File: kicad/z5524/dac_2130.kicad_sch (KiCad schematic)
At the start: 31 parts, among them U3 TL072, U4 AD5328

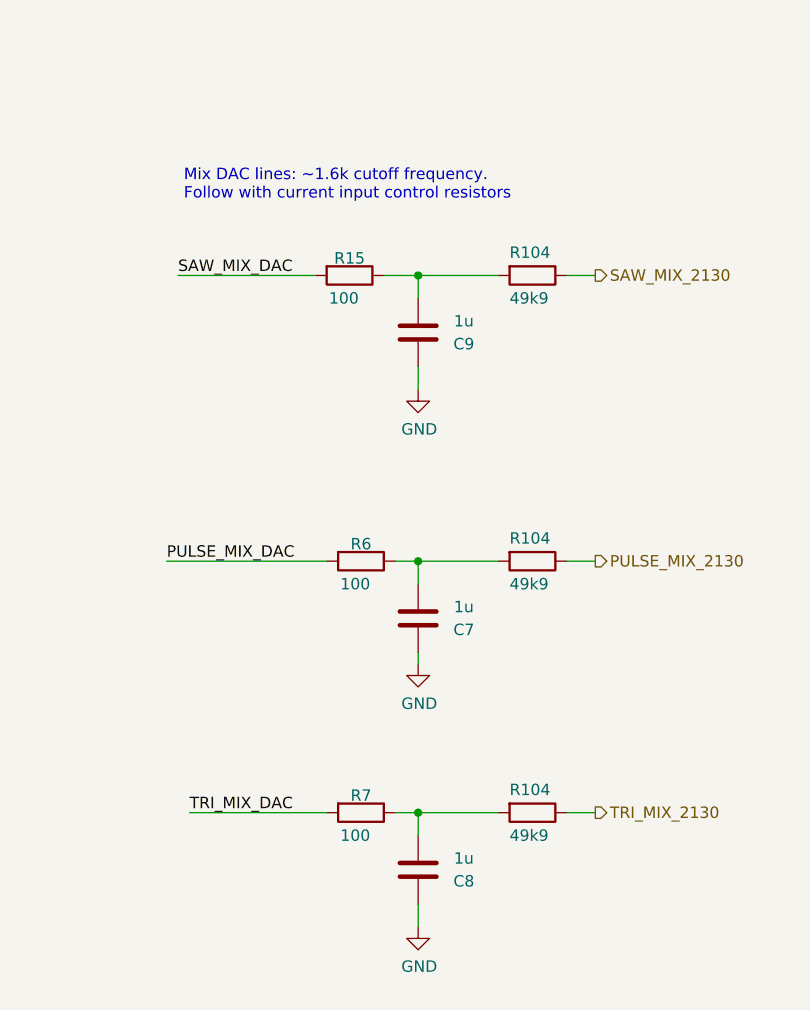
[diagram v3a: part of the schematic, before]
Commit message: updates to scale modulation values better
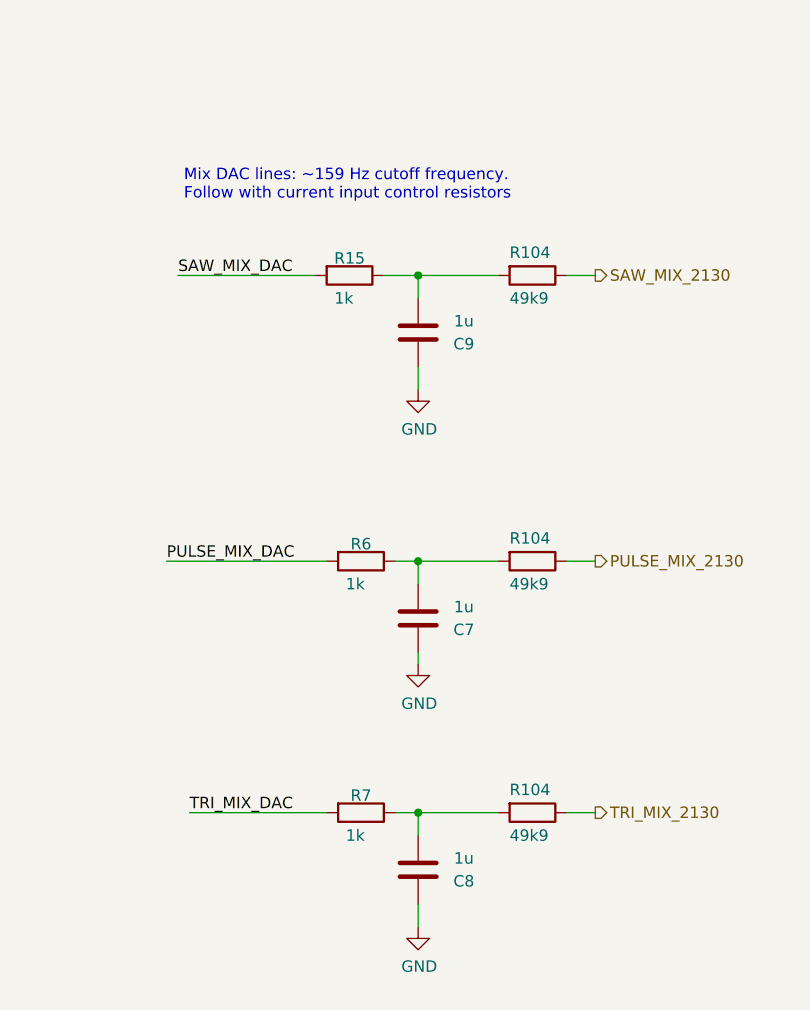
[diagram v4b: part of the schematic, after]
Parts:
- R15, R6, R7: value 100 -> 1k; LCSC C22775 -> C21190
- R17, R19: LCSC (none) -> C4184
- R18, R82: LCSC (none) -> C25804
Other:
- note added: "Mix DAC lines: ~159 Hz cutoff frequency. Follow with current input control resistors"
- note removed: "Mix DAC lines: ~1.6k cutoff frequency. Follow with current input control resistors"
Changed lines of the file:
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@@
     (effects (font (size 1.27 1.27)) (justify left bottom))
   )
-  (text "Mix DAC lines: ~1.6k cutoff frequency.\nFollow with current input control resistors"
+  (text "Mix DAC lines: ~159 Hz cutoff frequency.\nFollow with current input control resistors"
     (at 221.615 126.365 0)
     (effects (font (size 1.27 1.27)) (justify left bottom))
@@
       (effects (font (size 1.27 1.27)) hide)
     )
-    (property "LCSC" "" (at 59.69 202.565 90)
+    (property "LCSC" "C25804" (at 59.69 202.565 90)
       (effects (font (size 1.27 1.27)) hide)
     )
@@
       (effects (font (size 1.27 1.27)) hide)
     )
-    (property "LCSC" "" (at 53.34 194.31 90)
+    (property "LCSC" "C4184" (at 53.34 194.31 90)
       (effects (font (size 1.27 1.27)) hide)
     )
@@
       (effects (font (size 1.27 1.27)) hide)
     )
-    (property "LCSC" "" (at 57.15 181.61 0)
+    (property "LCSC" "C25804" (at 57.15 181.61 0)
       (effects (font (size 1.27 1.27)) hide)
     )
@@
       (effects (font (size 1.27 1.27)))
     )
-    (property "Value" "100" (at 240.665 196.85 90)
+    (property "Value" "1k" (at 240.665 196.85 90)
       (effects (font (size 1.27 1.27)))
     )
@@
       (effects (font (size 1.27 1.27)) hide)
     )
-    (property "LCSC" "C22775" (at 241.3 194.31 90)
+    (property "LCSC" "C21190" (at 241.3 194.31 90)
       (effects (font (size 1.27 1.27)) hide)
     )
@@
       (effects (font (size 1.27 1.27)) hide)
     )
-    (property "LCSC" "" (at 72.39 181.61 0)
+    (property "LCSC" "C4184" (at 72.39 181.61 0)
       (effects (font (size 1.27 1.27)) hide)
     )
@@
       (effects (font (size 1.27 1.27)))
     )
-    (property "Value" "100" (at 239.395 137.16 90)
+    (property "Value" "1k" (at 239.395 137.16 90)
       (effects (font (size 1.27 1.27)))
     )
@@
       (effects (font (size 1.27 1.27)) hide)
     )
-    (property "LCSC" "C22775" (at 240.03 134.62 90)
+    (property "LCSC" "C21190" (at 240.03 134.62 90)
       (effects (font (size 1.27 1.27)) hide)
     )
@@
       (effects (font (size 1.27 1.27)))
     )
-    (property "Value" "100" (at 240.665 168.91 90)
+    (property "Value" "1k" (at 240.665 168.91 90)
       (effects (font (size 1.27 1.27)))
     )
@@
       (effects (font (size 1.27 1.27)) hide)
     )
-    (property "LCSC" "C22775" (at 241.3 166.37 90)
-      (effects (font (size 1.27 1.27)) hide)
-    )
+    (property "LCSC" "C21190" (at 241.3 166.37 90)
+      (effects (font (size 1.27 1.27)) hide)
+    )

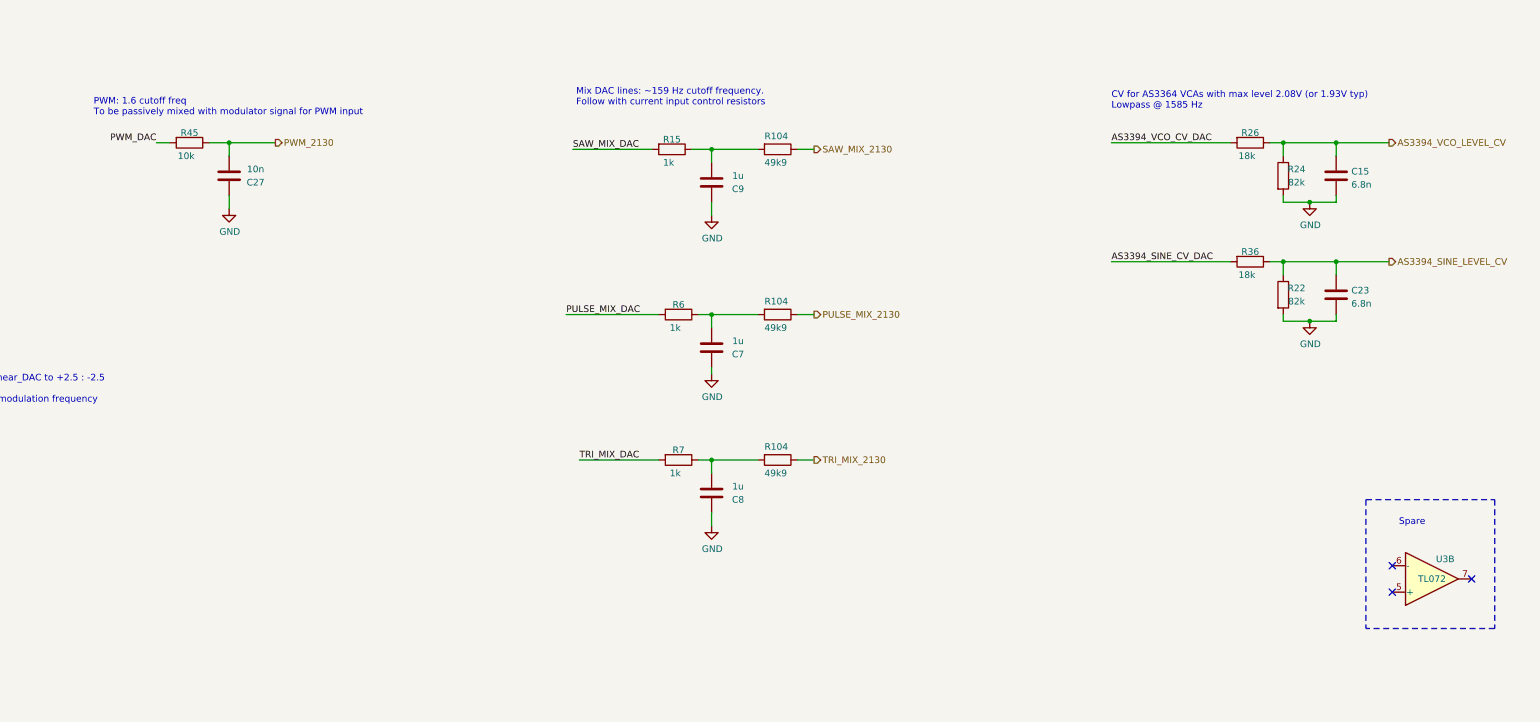
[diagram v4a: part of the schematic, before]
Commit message: schematic updates- cv values from dac and input protections between VCOs
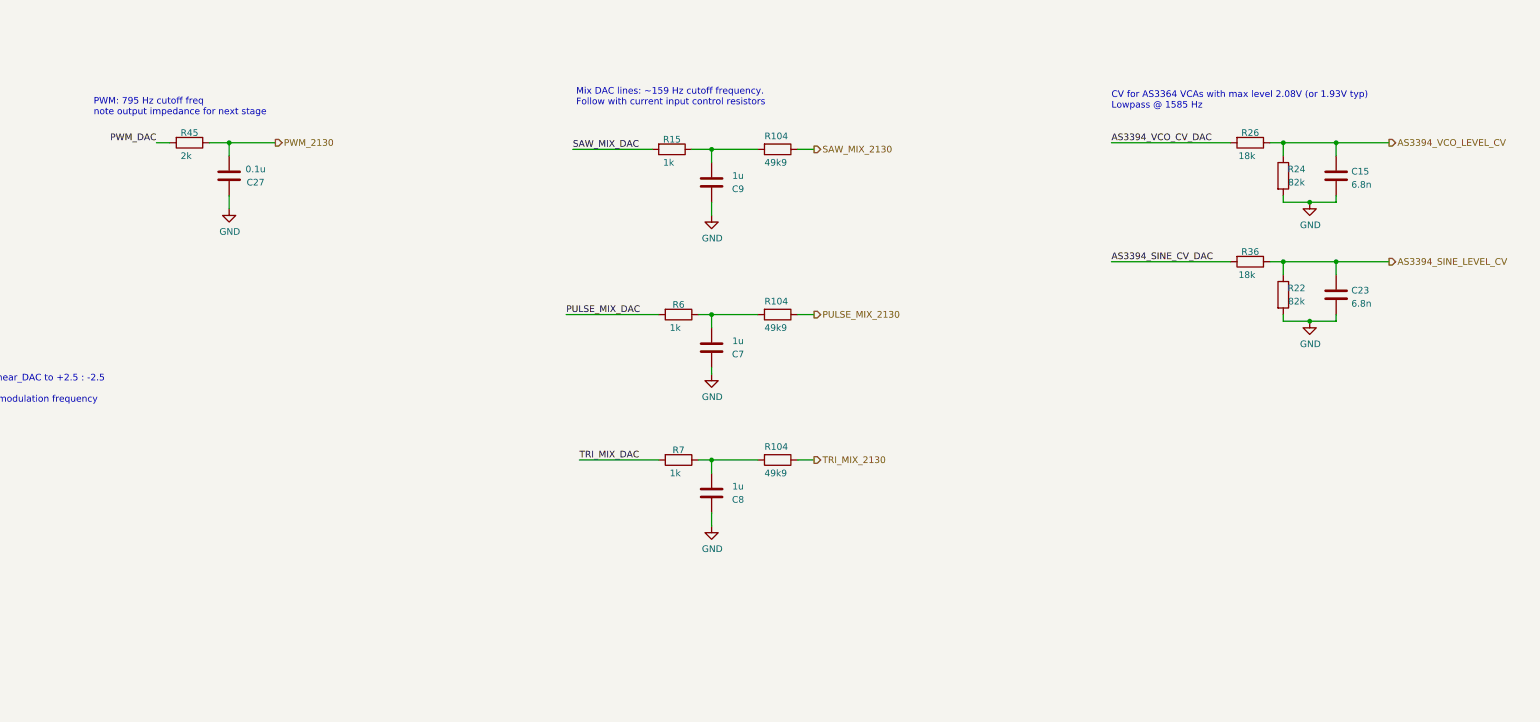
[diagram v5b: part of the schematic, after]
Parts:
- removed unit 2 of U3
- C27: value 10n -> 0.1u; LCSC C57112 -> (none)
- R109: LCSC C60590 -> C22809
- R45: value 10k -> 2k; LCSC C25804 -> C22975
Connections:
- no-connect marks 3 -> 0
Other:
- note added: "PWM: 795 Hz cutoff freq note output impedance for next stage"
- note removed: "PWM: 1.6 cutoff freq To be passively mixed with modulator signal for PWM input"
- note removed: "Spare"
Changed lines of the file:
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@@
   (junction (at 64.77 133.35) (diameter 0) (color 0 0 0 0)
   )
-  (no_connect (at 378.46 219.71))
-  (no_connect (at 393.7 217.17))
-  (no_connect (at 378.46 214.63))
   (wire (pts (xy 354.965 156.21) (xy 357.505 156.21))
     (stroke (width 0) (type default))
@@
     (stroke (width 0) (type default))
   )
-  (polyline (pts (xy 373.38 201.93) (xy 398.145 201.93))
-    (stroke (width 0) (type dash))
-  )
   (wire (pts (xy 357.505 133.35) (xy 357.505 135.89))
     (stroke (width 0) (type default))
@@
     (stroke (width 0) (type default))
   )
-  (polyline (pts (xy 398.145 201.93) (xy 398.145 226.695))
-    (stroke (width 0) (type dash))
-  )
   (wire (pts (xy 367.665 133.35) (xy 367.665 135.89))
     (stroke (width 0) (type default))
@@
     (stroke (width 0) (type default))
   )
-  (polyline (pts (xy 373.38 201.93) (xy 373.38 226.695))
-    (stroke (width 0) (type dash))
-  )
-  (polyline (pts (xy 398.145 226.695) (xy 373.38 226.695))
-    (stroke (width 0) (type dash))
-  )
   (wire (pts (xy 45.085 194.31) (xy 49.53 194.31))
     (stroke (width 0) (type default))
@@
     (stroke (width 0) (type default))
   )
-  (text "PWM: 1.6 cutoff freq\nTo be passively mixed with modulator signal for PWM input"
+  (text "PWM: 795 Hz cutoff freq\nnote output impedance for next stage"
     (at 128.905 128.27 0)
     (effects (font (size 1.27 1.27)) (justify left bottom))
@@
   )
   (text "Sheet load:\nVref_2.5: 45k || 30k ==> 18k\n" (at 157.48 22.86 0)
-    (effects (font (size 1.27 1.27)) (justify left bottom))
-  )
-  (text "Spare" (at 379.73 207.01 0)
     (effects (font (size 1.27 1.27)) (justify left bottom))
   )
@@
       (effects (font (size 1.27 1.27)))
     )
-    (property "Value" "10k" (at 146.685 135.89 90)
+    (property "Value" "2k" (at 146.685 135.89 90)
       (effects (font (size 1.27 1.27)))
     )
@@
       (effects (font (size 1.27 1.27)) hide)
     )
-    (property "LCSC" "C25804" (at 147.32 133.35 0)
+    (property "LCSC" "C22975" (at 147.32 133.35 0)
       (effects (font (size 1.27 1.27)) hide)
     )
@@
     )
   )
-  (symbol (lib_id "Amplifier_Operational:TL072") (at 386.08 217.17 0) (mirror x) (unit 2)
-    (in_bom yes) (on_board yes) (dnp no)
-    (property "Reference" "U3" (at 388.62 213.36 0)
-      (effects (font (size 1.27 1.27)))
-    )
-    (property "Value" "TL072" (at 386.08 217.17 0)
-      (effects (font (size 1.27 1.27)))
-    )
-    (property "Footprint" "Package_SO:SO-8_3.9x4.9mm_P1.27mm" (at 386.08 217.17 0)
-      (effects (font (size 1.27 1.27)) hide)
-    )
-    (property "Datasheet" "http://www.ti.com/lit/ds/symlink/tl071.pdf" (at 386.08 217.17 0)
-      (effects (font (size 1.27 1.27)) hide)
-    )
-    (property "LCSC" "C6961" (at 386.08 217.17 0)
-      (effects (font (size 1.27 1.27)) hide)
-    )
-    (pin "1")
-    (pin "2")
-    (pin "3")
-    (pin "5")
-    (pin "6")
-    (pin "7")
-    (pin "4")
-    (pin "8")
-    (instances
-      (project "z5524"
-        (path "/7079bdb0-a00e-4bac-b257-cbcf2c91bbd6/00000000-0000-0000-0000-000061ff2290"
-          (reference "U3") (unit 2)
-        )
-      )
-    )
-  )
   (symbol (lib_id "Device:R") (at 74.93 133.35 270) (unit 1)
     (in_bom yes) (on_board yes) (dnp no)
@@
       (effects (font (size 1.27 1.27)) hide)
     )
-    (property "LCSC" "C60590" (at 74.93 133.35 0)
+    (property "LCSC" "C22809" (at 74.93 133.35 0)
       (effects (font (size 1.27 1.27)) hide)
     )
@@
       (effects (font (size 1.27 1.27)))
     )
-    (property "Value" "10n" (at 160.02 138.43 0)
+    (property "Value" "0.1u" (at 160.02 138.43 0)
       (effects (font (size 1.27 1.27)))
     )
@@
       (effects (font (size 1.27 1.27)) hide)
     )
-    (property "LCSC" "C57112" (at 154.94 139.7 90)
-      (effects (font (size 1.27 1.27)) hide)
-    )
+    (property "LCSC" "" (at 154.94 139.7 90)
+      (effects (font (size 1.27 1.27)) hide)
+    )

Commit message: routed - initial at least
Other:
- note added: "VCO Pitch: From 2.5V source, a 20 uA/octave source for 8 octaves gives 15625 for R. Divide this to a low impedance LPF section with a ~1200 Hz filter. No R value needed on SSI2130 sheet."
- note removed: "VCO Pitch: From 2.5V source, a 20 uA/octave source for 8 octaves gives 15625 for R. Divide this to a low impedance LPF section with a ~1200 Hz filter"
- title: Zoxnoxious SSI2130/AS3394 -> Zoxnoxious Z5524 (SSI2130/AS3394)
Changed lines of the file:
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@@
   (paper "B")
   (title_block
-    (title "Zoxnoxious SSI2130/AS3394")
-    (date "2023-08-27")
-    (rev "0.2")
+    (title "Zoxnoxious Z5524 (SSI2130/AS3394)")
+    (date "2023-12-06")
+    (rev "0.3")
     (company "Zoxnoxious Engineering")
   )
@@
     (effects (font (size 1.27 1.27)) (justify left bottom))
   )
-  (text "VCO Pitch:\nFrom 2.5V source, a 20 uA/octave\nsource for 8 octaves gives 15625 for R.\nDivide this to a low impedance LPF section\nwith a ~1200 Hz filter"
+  (text "VCO Pitch:\nFrom 2.5V source, a 20 uA/octave\nsource for 8 octaves gives 15625 for R.\nDivide this to a low impedance LPF section\nwith a ~1200 Hz filter.\nNo R value needed on SSI2130 sheet."
     (at 36.83 123.825 0)
     (effects (font (size 1.27 1.27)) (justify left bottom))
